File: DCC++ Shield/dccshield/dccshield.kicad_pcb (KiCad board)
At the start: 2 copper layers, 6 parts, among them Q1 BTN8982TA, Q2 BTN8982TA, U1 74HC04, U2 A4953_LJ

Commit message: Update
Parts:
- removed REF**: TerminalBlock_bornier-6_P5.08mm, Connectors_Terminal_Blocks:TerminalBlock_bornier-6_P5.08mm
- added J1: Conn_01x06, Connectors_Terminal_Blocks:TerminalBlock_bornier-6_P5.08mm, F.Cu at (185.4, 91.4)
- added R1: 10K, Resistors_SMD:R_0805, F.Cu at (180.3, 123.5)
- added R10: 10K, Resistors_SMD:R_0805, F.Cu at (171.4, 82.5)
- added R11: DNF, Resistors_SMD:R_0805, F.Cu at (182.9, 123.5)
- added R12: DNF, Resistors_SMD:R_0805, F.Cu at (156.0, 123.5)
- added R2: 10K, Resistors_SMD:R_0805, F.Cu at (161.0, 123.5)
- added R3: 10K, Resistors_SMD:R_0805, F.Cu at (166.4, 123.2)
- added R4: 1K, Resistors_SMD:R_0805, F.Cu at (157.5, 95.2)
- added R5: 1K, Resistors_SMD:R_0805, F.Cu at (157.5, 108.0)
- added R6: 1K, Resistors_SMD:R_0805, F.Cu at (183.5, 83.8)
- added R7: TBD, Resistors_SMD:R_0805, F.Cu at (157.5, 100.3)
- added R8: 10K, Resistors_SMD:R_0805, F.Cu at (181.6, 83.8)
- added R9: 1K, Resistors_SMD:R_0805, F.Cu at (169.5, 82.5)
- added Rs1: 0R25 1% 1W, Resistors_SMD:R_2512, F.Cu at (177.8, 133.3)
- added U3: LM358, Housings_SOIC:SOIC-8_3.9x4.9mm_Pitch1.27mm, F.Cu at (176.5, 83.8)
- moved U1 11.3 mm to (151.1, 107.3), turned to 180 degrees
- moved Q2 8.98 mm to (168.9, 108.0)
- moved Q1 8.98 mm to (168.9, 95.2)
- moved U2 1.80 mm to (174.0, 118.1)
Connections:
- A1 pad 10: Net-(A1-Pad10) -> /A1
- A1 pad 18: Net-(A1-Pad18) -> /ENABLE_MAIN
- A1 pad 20: Net-(A1-Pad20) -> /DCC_SIGNAL_PROG
- A1 pad 25: Net-(A1-Pad25) -> /DCC_SIGNAL_MAIN
- A1 pad 29: Net-(A1-Pad29) -> GND
- A1 pad 30: Net-(A1-Pad30) -> +5V
- A1 pad 5: Net-(A1-Pad5) -> +5V
- A1 pad 6: Net-(A1-Pad6) -> GND
- A1 pad 7: Net-(A1-Pad7) -> GND
- A1 pad 9: Net-(A1-Pad9) -> /A0
- Q2 pad 3: Net-(Q2-Pad3) -> Net-(Q1-Pad3)
- Q2 pad 6: Net-(Q2-Pad6) -> Net-(Q1-Pad6)
- U1 pad 14: Net-(U1-Pad14) -> +5V
- U1 pad 2: Net-(U1-Pad2) -> Net-(Q1-Pad3)
- U1 pad 3: (no net) -> Net-(R3-Pad1)
- U1 pad 4: (no net) -> Net-(U1-Pad4)
- U1 pad 5: (no net) -> Net-(Q1-Pad2)
- U1 pad 6: (no net) -> Net-(Q2-Pad2)
- U1 pad 7: Net-(U1-Pad7) -> GND
- U2 pad 2: Net-(U2-Pad2) -> Net-(U1-Pad4)
- U2 pad 3: Net-(U2-Pad3) -> Net-(R3-Pad1)
- U2 pad 4: Net-(U2-Pad4) -> +5V
- U2 pad 6: PROG1 -> PROG2
- U2 pad 8: PROG2 -> PROG1
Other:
- board outline added: 57.2 x 53.3 mm

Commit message: PCB update
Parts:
- added C1: 100nF, Capacitors_SMD:C_0805, F.Cu at (182.2, 81.3)
- added C2: 100nF, Capacitors_SMD:C_0805, F.Cu at (152.5, 113.0)
- added C3: 100nF, Capacitors_SMD:C_0805, F.Cu at (167.0, 123.2)
- added C4: 100nF, Capacitors_SMD:C_0805, F.Cu at (173.4, 123.2)
- added C5: DNF, Capacitors_SMD:C_0805, F.Cu at (170.2, 85.1)
- added C6: 100uF 50V, Capacitors_SMD:CP_Elec_6.3x5.3, F.Cu at (162.6, 85.7)
- added R13: TBD, Resistors_SMD:R_0805, F.Cu at (160.0, 98.4)
- added R14: DNF, Resistors_SMD:R_0805, F.Cu at (160.0, 101.6)
- moved Rs1 12.8 mm to (176.5, 120.7), turned to 270 degrees
- moved R7 11.1 mm to (160.0, 111.1)
- moved R3 9.67 mm to (162.6, 132.1)
- moved U2 3.81 mm to (170.2, 118.1)
- moved R4 2.84 mm to (160.0, 96.5)
- moved R5 2.84 mm to (160.0, 109.2)
- moved Q1 1.27 mm to (170.2, 95.2)
- moved Q2 1.27 mm to (170.2, 108.0)
- moved U1 1.27 mm to (152.4, 107.3)
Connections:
- Q1 pad 6: Net-(Q1-Pad6) -> Net-(C5-Pad1)
- Q2 pad 6: Net-(Q1-Pad6) -> Net-(Q2-Pad6)
- R7 pad 2: Net-(Q1-Pad6) -> Net-(Q2-Pad6)
- U3 pad 3: Net-(Q1-Pad6) -> Net-(C5-Pad1)
- U3 pad 8: Net-(U3-Pad8) -> +5V
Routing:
- net Net-(Rs1-Pad1): track 0.00 -> 56.8 mm, vias 0 -> 2
- net Net-(Q1-Pad2): track 0.00 -> 25.3 mm
- net MAIN1: track 0.00 -> 22.4 mm
- net MAIN2: track 0.00 -> 22.1 mm
- net Net-(Q1-Pad3): track 0.00 -> 16.6 mm
- net PROG1: track 0.00 -> 14.9 mm
- net PROG2: track 0.00 -> 13.9 mm
- net Net-(Q2-Pad2): track 0.00 -> 9.57 mm
- net /A1: track 0.00 -> 8.29 mm
- net /A0: track 0.00 -> 7.02 mm
- net GND: track 0.00 -> 4.84 mm, vias 0 -> 12
- net Net-(R10-Pad2): track 0.00 -> 4.42 mm
- net Net-(R6-Pad2): track 0.00 -> 4.42 mm
- net Net-(Q2-Pad6): track 0.00 -> 3.70 mm
- net Net-(C5-Pad1): track 0.00 -> 3.70 mm
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- added copper zone on B.Cu, net VCC
- added copper zone on F.Cu, net VCC
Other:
- rule via_min_drill: 0.3 -> 0.4
- rule via_min_size: 0.4 -> 0.7

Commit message: Up
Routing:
- net +5V: track 2.37 -> 0.00 mm, vias 1 -> 0
- net VCC: vias 11 -> 12
- net GND: vias 12 -> 23
- added copper zone on F.Cu, net +5V
- added copper zone on B.Cu, net GND
- added copper zone on F.Cu, net GND
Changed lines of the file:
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@@
     (thickness 1.6)
     (drawings 9)
-    (tracks 119)
+    (tracks 127)
     (zones 0)
     (modules 28)
@@
   (via (at 158.115 98.425) (size 0.8) (drill 0.4) (layers F.Cu B.Cu) (net 29))
   (segment (start 159.07 98.425) (end 158.115 98.425) (width 0.5) (layer F.Cu) (net 29))
+  (via (at 162.56 102.87) (size 0.8) (drill 0.4) (layers F.Cu B.Cu) (net 29))
+  (via (at 163.83 102.87) (size 0.8) (drill 0.4) (layers F.Cu B.Cu) (net 29))
+  (via (at 165.1 102.87) (size 0.8) (drill 0.4) (layers F.Cu B.Cu) (net 29))
+  (via (at 166.37 102.87) (size 0.8) (drill 0.4) (layers F.Cu B.Cu) (net 29))
+  (via (at 166.37 90.17) (size 0.8) (drill 0.4) (layers F.Cu B.Cu) (net 29))
+  (via (at 162.56 90.17) (size 0.8) (drill 0.4) (layers F.Cu B.Cu) (net 29))
+  (via (at 163.83 90.17) (size 0.8) (drill 0.4) (layers F.Cu B.Cu) (net 29))
+  (via (at 165.1 90.17) (size 0.8) (drill 0.4) (layers F.Cu B.Cu) (net 29))
+  (via (at 169.545 114.935) (size 0.8) (drill 0.4) (layers F.Cu B.Cu) (net 29))
+  (via (at 170.815 114.935) (size 0.8) (drill 0.4) (layers F.Cu B.Cu) (net 29))
+  (via (at 173.355 125.095) (size 0.8) (drill 0.4) (layers F.Cu B.Cu) (net 29))
   (segment (start 164.405 95.25) (end 173.555 95.25) (width 1) (layer F.Cu) (net 30))
   (segment (start 173.555 95.25) (end 175.895 95.25) (width 2) (layer F.Cu) (net 30))
@@
   (via (at 173.355 121.285) (size 0.8) (drill 0.4) (layers F.Cu B.Cu) (net 31))
   (via (at 174.625 121.285) (size 0.8) (drill 0.4) (layers F.Cu B.Cu) (net 31))
+  (via (at 172.085 122.555) (size 0.8) (drill 0.4) (layers F.Cu B.Cu) (net 31))
   (segment (start 164.405 107.95) (end 173.555 107.95) (width 1) (layer F.Cu) (net 32))
   (segment (start 174.825 106.68) (end 173.555 107.95) (width 2) (layer F.Cu) (net 32))
@@
   (segment (start 172.88 118.745) (end 173.99 118.745) (width 0.5) (layer F.Cu) (net 34))
   (segment (start 173.99 118.745) (end 174.625 119.38) (width 0.5) (layer F.Cu) (net 34))
-  (via (at 167.005 121.285) (size 0.8) (drill 0.4) (layers F.Cu B.Cu) (net 35))
-  (segment (start 167.005 122.19) (end 167.005 121.285) (width 1) (layer F.Cu) (net 35))
-  (segment (start 167.48 120.81) (end 167.005 121.285) (width 0.5) (layer F.Cu) (net 35))
-  (segment (start 167.48 120.015) (end 167.48 120.81) (width 0.5) (layer F.Cu) (net 35))
   (via (at 180.34 121.66599) (size 0.8) (drill 0.4) (layers F.Cu B.Cu) (net 36))
   (segment (start 180.34 122.56) (end 180.34 121.66599) (width 0.3) (layer F.Cu) (net 36))
@@
     (polygon
       (pts
-        (xy 188.86317 93.98) (xy 175.26 93.98) (xy 175.26 122.555) (xy 171.45 122.555) (xy 171.45 114.3)
-        (xy 161.29 114.3) (xy 161.29 95.25) (xy 154.94 95.25) (xy 154.94 88.9) (xy 188.86317 88.9)
+        (xy 188.595 93.345) (xy 175.26 93.345) (xy 170.815 88.9) (xy 161.29 88.9) (xy 161.29 95.25)
+        (xy 167.64 95.25) (xy 167.64 100.965) (xy 161.925 100.965) (xy 161.925 107.95) (xy 168.275 107.95)
+        (xy 168.275 114.3) (xy 168.275 120.65) (xy 175.26 120.65) (xy 175.26 123.825) (xy 161.925 123.825)
+        (xy 161.925 114.3) (xy 158.115 114.3) (xy 158.115 101.6) (xy 154.94 101.6) (xy 154.94 86.995)
+        (xy 180.34 86.995) (xy 181.61 88.265) (xy 188.595 88.265)
       )
     )
@@
     (polygon
       (pts
-        (xy 175.26 123.19) (xy 171.45 123.19) (xy 171.45 119.38) (xy 175.26 119.38)
+        (xy 175.26 123.19) (xy 172.085 123.19) (xy 172.085 119.38) (xy 175.26 119.38)
       )
     )
+  )
+  (zone (net 29) (net_name GND) (layer F.Cu) (hatch edge 0.508)
+    (priority 1)
+    (connect_pads yes (clearance 0.508))
+    (min_thickness 0.254)
+    (fill yes (arc_segments 32) (thermal_gap 0.508) (thermal_bridge_width 0.508))
+    (polygon
+      (pts
+        (xy 167.005 104.775) (xy 161.925 104.775) (xy 161.925 102.235) (xy 167.005 102.235)
+      )
+    )
+  )
+  (zone (net 29) (net_name GND) (layer F.Cu) (hatch edge 0.508)
+    (priority 1)
+    (connect_pads yes (clearance 0.508))
+    (min_thickness 0.254)
+    (fill yes (arc_segments 32) (thermal_gap 0.508) (thermal_bridge_width 0.508))
+    (polygon
+      (pts
+        (xy 166.9678 92.075) (xy 161.8878 92.075) (xy 161.8878 89.535) (xy 166.9678 89.535)
+      )
+    )
+  )
+  (zone (net 31) (net_name VCC) (layer F.Cu) (hatch edge 0.508)
+    (priority 1)
+    (connect_pads yes (clearance 0.508))
+    (min_thickness 0.254)
+    (fill yes (arc_segments 32) (thermal_gap 0.508) (thermal_bridge_width 0.508))
+    (polygon
+      (pts
+        (xy 167.005 113.665) (xy 161.925 113.665) (xy 161.925 111.125) (xy 167.005 111.125)
+      )
+    )
+  )
+  (zone (net 31) (net_name VCC) (layer F.Cu) (hatch edge 0.508)
+    (priority 1)
+    (connect_pads yes (clearance 0.508))
+    (min_thickness 0.254)
+    (fill yes (arc_segments 32) (thermal_gap 0.508) (thermal_bridge_width 0.508))
+    (polygon
+      (pts
+        (xy 167.005 100.965) (xy 161.925 100.965) (xy 161.925 98.425) (xy 167.005 98.425)
+      )
+    )
+  )
+  (zone (net 29) (net_name GND) (layer B.Cu) (hatch edge 0.508)
+    (connect_pads yes (clearance 0.508))
+    (min_thickness 0.254)
+    (fill yes (arc_segments 32) (thermal_gap 0.508) (thermal_bridge_width 0.508))
+    (polygon
+      (pts
+        (xy 170.4975 89.535) (xy 174.9425 93.98) (xy 188.595 93.98) (xy 188.595 99.06) (xy 175.26 99.06)
+        (xy 175.26 116.84) (xy 178.435 120.015) (xy 178.435 125.73) (xy 172.72 125.73) (xy 172.72 124.46)
+        (xy 175.26 124.46) (xy 175.26 120.65) (xy 168.91 120.65) (xy 168.91 107.315) (xy 161.925 107.315)
+        (xy 161.925 101.6) (xy 168.275 101.6) (xy 168.275 94.615) (xy 161.925 94.615) (xy 161.925 89.535)
+      )
+    )
+  )
+  (zone (net 29) (net_name GND) (layer F.Cu) (hatch edge 0.508)
+    (connect_pads yes (clearance 0.508))
+    (min_thickness 0.254)
+    (fill yes (arc_segments 32) (thermal_gap 0.508) (thermal_bridge_width 0.508))
+    (polygon
+      (pts
+        (xy 171.45 123.19) (xy 168.91 123.19) (xy 168.91 116.84) (xy 161.925 116.84) (xy 161.925 114.3)
+        (xy 171.45 114.3)
+      )
+    )
+  )
+  (zone (net 29) (net_name GND) (layer F.Cu) (hatch edge 0.508)
+    (connect_pads yes (clearance 0.508))
+    (min_thickness 0.254)
+    (fill yes (arc_segments 32) (thermal_gap 0.508) (thermal_bridge_width 0.508))
+    (polygon
+      (pts
+        (xy 178.435 125.73) (xy 172.085 125.73) (xy 172.085 123.19) (xy 178.435 123.19)
+      )
+    )
+  )
+  (zone (net 35) (net_name +5V) (layer F.Cu) (hatch edge 0.508)
+    (connect_pads yes (clearance 0.508))
+    (min_thickness 0.254)
+    (fill yes (arc_segments 32) (thermal_gap 0.508) (thermal_bridge_width 0.508))
+    (polygon
+      (pts
+        (xy 163.83 82.55) (xy 147.32 82.55) (xy 147.32 114.3) (xy 142.24 114.3) (xy 142.24 80.01)
+        (xy 161.29 80.01) (xy 161.29 77.47) (xy 163.83 77.47)
+      )
+    )

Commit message: PCB update
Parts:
- moved R1 27.5 mm to (154.9, 113.0), turned to 0 degrees
- moved C3 18.9 mm to (148.3, 120.4), turned to 90 degrees
- moved R11 16.8 mm to (166.1, 123.4), turned to 270 degrees
- moved R3 8.70 mm to (163.6, 123.4)
- moved R4 5.85 mm to (158.8, 102.2), turned to 90 degrees
- moved R5 5.24 mm to (158.8, 114.3), turned to 90 degrees
- moved R14 5.12 mm to (155.6, 99.1)
- moved R13 3.86 mm to (160.7, 102.2), turned to 90 degrees
- moved C5 3.59 mm to (167.6, 82.5), turned to 90 degrees
- moved R7 3.24 mm to (160.7, 114.3), turned to 90 degrees
- moved C2 2.93 mm to (149.9, 114.3), turned to 270 degrees
- moved C6 1.42 mm to (161.9, 87.0), turned to 180 degrees
- turned R2 to 90 degrees
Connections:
- A1 pad 25: /DCC_SIGNAL_MAIN -> Net-(A1-Pad25)
- Q1 pad 2: Net-(Q1-Pad2) -> /DCC_SIGNAL_MAIN
- R2 pad 1: Net-(Q1-Pad2) -> Net-(A1-Pad25)
- U1 pad 5: Net-(Q1-Pad2) -> /DCC_SIGNAL_MAIN
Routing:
- net /DCC_SIGNAL_MAIN: track 2.54 -> 55.4 mm, vias 0 -> 2
- net +5V: track 0.00 -> 50.6 mm, vias 0 -> 1
- net Net-(R3-Pad1): track 0.00 -> 35.1 mm, vias 0 -> 2
- net /ENABLE_MAIN: track 2.54 -> 34.5 mm, vias 0 -> 1
- net Net-(C5-Pad1): track 3.70 -> 33.5 mm, vias 0 -> 1
- net Net-(Q2-Pad6): track 3.70 -> 32.1 mm, vias 0 -> 2
- net Net-(U1-Pad4): track 0.00 -> 25.7 mm, vias 0 -> 2
- net Net-(Q1-Pad2): track 25.3 -> 0.00 mm
- net Net-(Q1-Pad3): track 16.6 -> 40.2 mm, vias 0 -> 2
- net Net-(A1-Pad17): track 2.54 -> 18.9 mm, vias 0 -> 1
- net /DCC_SIGNAL_PROG: track 0.89 -> 14.8 mm, vias 1 -> 0
- net Net-(Q1-Pad5): track 3.44 -> 9.03 mm
- net Net-(Q2-Pad5): track 3.44 -> 8.30 mm
- net GND: track 4.84 -> 8.77 mm, vias 23 -> 29
- net Net-(A1-Pad25): track 0.00 -> 2.54 mm
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
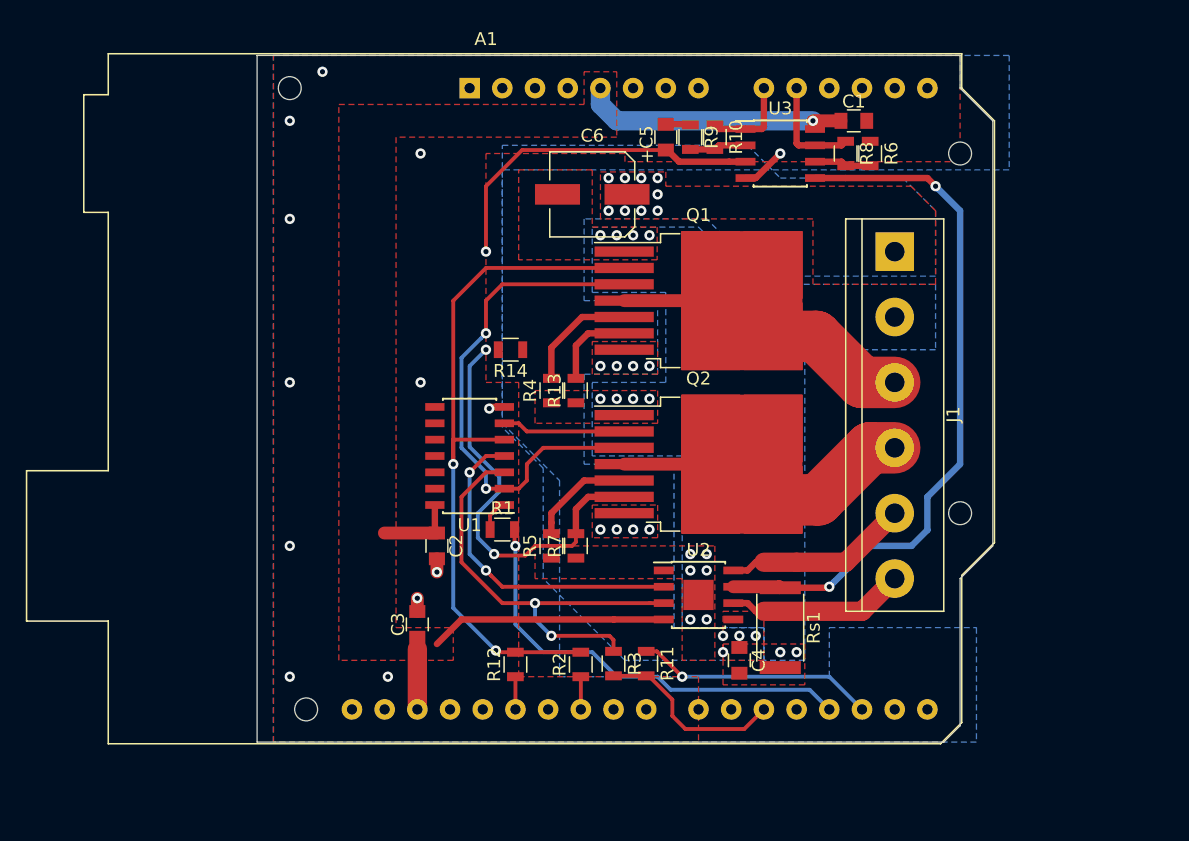
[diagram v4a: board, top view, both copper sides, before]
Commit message: 3d models added
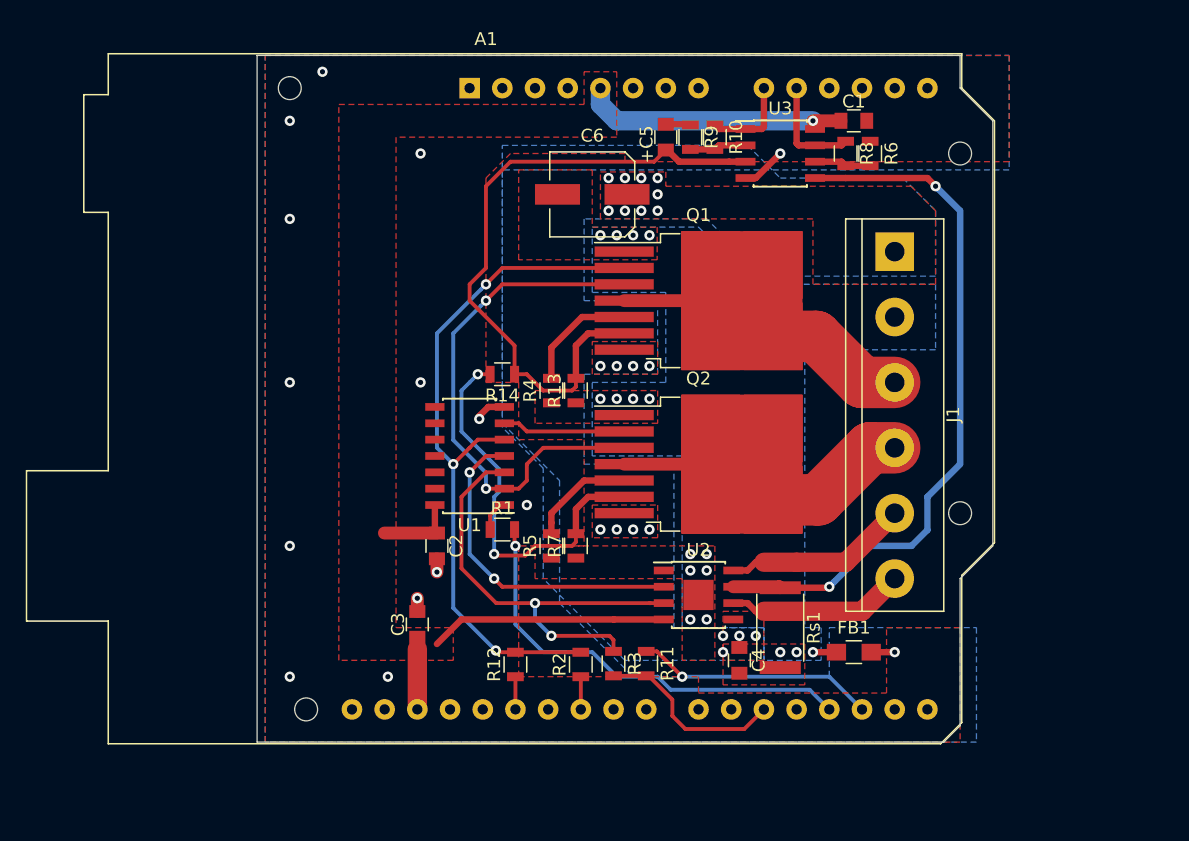
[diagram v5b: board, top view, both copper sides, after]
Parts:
- added FB1: Ferrite_Bead_Small, Inductors_SMD:L_0805_HandSoldering, F.Cu at (182.2, 122.6)
- moved R14 2.01 mm to (154.9, 101.0)
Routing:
- net Net-(C5-Pad1): track 33.5 -> 51.0 mm, vias 1 -> 0
- net GND: track 8.77 -> 13.7 mm, vias 29 -> 32
- net Net-(Q2-Pad6): track 32.1 -> 30.4 mm
- net /DCC_SIGNAL_MAIN: track 55.4 -> 54.6 mm, vias 2 -> 3
- net Net-(Q1-Pad3): track 40.2 -> 40.8 mm
